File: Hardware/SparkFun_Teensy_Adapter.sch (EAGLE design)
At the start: 17 parts, among them U1 5V

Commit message: Updates for QC final review before reds
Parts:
- FRAME1: VERSION (none) -> v10
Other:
- note added: "v10"
- note removed: "v01"
- moved on the sheet: SJ1, SJ2
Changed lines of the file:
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@@
 <part name="FRAME1" library="SparkFun-Aesthetics" deviceset="FRAME-LETTER" device="">
 <attribute name="DESIGNER" value="Toni Klopfenstein"/>
+<attribute name="VERSION" value="v10"/>
 </part>
 <part name="LOGO1" library="SparkFun-Aesthetics" deviceset="SFE_LOGO_NAME_FLAME" device=".1_INCH"/>
@@
 <part name="GND10" library="SparkFun-Aesthetics" deviceset="GND" device=""/>
 <part name="U1" library="SparkFun-PowerIC" deviceset="V_REG_78XX" device="-TO-220" value="5V"/>
+<part name="SUPPLY1" library="SparkFun-Aesthetics" deviceset="5V" device=""/>
+<part name="SUPPLY2" library="SparkFun-Aesthetics" deviceset="5V" device=""/>
+<part name="SUPPLY3" library="SparkFun-Aesthetics" deviceset="5V" device=""/>
+<part name="SUPPLY4" library="SparkFun-Aesthetics" deviceset="3.3V" device=""/>
+<part name="SUPPLY5" library="SparkFun-Aesthetics" deviceset="3.3V" device=""/>
+<part name="SUPPLY6" library="SparkFun-Aesthetics" deviceset="3.3V" device=""/>
+<part name="SUPPLY7" library="SparkFun-Aesthetics" deviceset="3.3V" device=""/>
 </parts>
 <sheets>
@@
 <text x="157.48" y="170.18" size="1.4224" layer="97">Add 32.768kHZ crystal
 to Teensy for use of RTC.  </text>
-<text x="2.54" y="142.24" size="1.27" layer="97">Cut trace between VUSB and VIN pads
- on Teensy to use external power supply. </text>
-<text x="5.08" y="76.2" size="1.778" layer="97">Jumpers default
+<text x="2.54" y="134.62" size="1.778" layer="97">Cut trace between
+ VUSB and VIN pads
+ on Teensy to use
+external power supply. </text>
+<text x="7.62" y="68.58" size="1.778" layer="97">Jumpers default
 to SDA/SCL.
 Can be adjusted to
-A6/A7 for Leonardo-compatible shields.</text>
+A6/A7 for
+Leonardo-compatible shields.</text>
 <wire x1="142.24" y1="185.42" x2="147.32" y2="185.42" width="0.2032" layer="97" style="shortdash"/>
 <wire x1="147.32" y1="185.42" x2="147.32" y2="147.32" width="0.2032" layer="97" style="shortdash"/>
@@
 <wire x1="106.68" y1="185.42" x2="106.68" y2="127" width="0.2032" layer="97" style="shortdash"/>
 <text x="116.84" y="129.54" size="2.54" layer="97">RTC Battery</text>
-<text x="238.76" y="7.62" size="2.54" layer="94">v01</text>
-<text x="172.72" y="10.16" size="2.54" layer="94">Toni Klopfenstein</text>
+<text x="238.76" y="7.62" size="2.54" layer="94">v10</text>
+<text x="171.958" y="10.922" size="2.54" layer="94">Toni Klopfenstein</text>
 </plain>
 <instances>
@@
 <instance part="GND2" gate="1" x="170.18" y="68.58"/>
 <instance part="GND3" gate="1" x="58.42" y="15.24"/>
-<instance part="SJ1" gate="G$1" x="30.48" y="104.14" smashed="yes" rot="R180">
-<attribute name="NAME" x="27.94" y="103.759" size="1.778" layer="95" rot="R180"/>
-</instance>
-<instance part="SJ2" gate="G$1" x="45.72" y="93.98" smashed="yes" rot="R180">
-<attribute name="NAME" x="43.18" y="93.599" size="1.778" layer="95" rot="R180"/>
+<instance part="SJ1" gate="G$1" x="20.32" y="104.14" smashed="yes" rot="R180">
+<attribute name="NAME" x="17.78" y="103.759" size="1.778" layer="95" rot="R180"/>
+</instance>
+<instance part="SJ2" gate="G$1" x="35.56" y="93.98" smashed="yes" rot="R180">
+<attribute name="NAME" x="33.02" y="93.599" size="1.778" layer="95" rot="R180"/>
 </instance>
 <instance part="JP2" gate="G$1" x="20.32" y="147.32" smashed="yes">
@@
 <instance part="GND10" gate="1" x="129.54" y="17.78"/>
 <instance part="U1" gate="G$1" x="68.58" y="154.94"/>
+<instance part="SUPPLY1" gate="G$1" x="83.82" y="157.48"/>
+<instance part="SUPPLY2" gate="G$1" x="45.72" y="88.9"/>
+<instance part="SUPPLY3" gate="G$1" x="157.48" y="99.06"/>
+<instance part="SUPPLY4" gate="G$1" x="25.4" y="175.26"/>
+<instance part="SUPPLY5" gate="G$1" x="40.64" y="86.36"/>
+<instance part="SUPPLY6" gate="G$1" x="60.96" y="33.02"/>
+<instance part="SUPPLY7" gate="G$1" x="152.4" y="93.98"/>
 </instances>
 <busses>
@@
 <segment>
 <pinref part="SJ2" gate="G$1" pin="3"/>
-<wire x1="45.72" y1="99.06" x2="45.72" y2="101.6" width="0.1524" layer="91"/>
-<wire x1="45.72" y1="101.6" x2="40.64" y2="101.6" width="0.1524" layer="91"/>
-<label x="40.64" y="101.6" size="1.27" layer="95" rot="R180" xref="yes"/>
+<wire x1="35.56" y1="99.06" x2="35.56" y2="101.6" width="0.1524" layer="91"/>
+<wire x1="35.56" y1="101.6" x2="30.48" y2="101.6" width="0.1524" layer="91"/>
+<label x="30.48" y="101.6" size="1.27" layer="95" rot="R180" xref="yes"/>
 </segment>
 </net>
@@
 <segment>
 <pinref part="SJ1" gate="G$1" pin="3"/>
-<wire x1="30.48" y1="109.22" x2="30.48" y2="111.76" width="0.1524" layer="91"/>
-<wire x1="30.48" y1="111.76" x2="25.4" y2="111.76" width="0.1524" layer="91"/>
-<label x="25.4" y="111.76" size="1.27" layer="95" rot="R180" xref="yes"/>
+<wire x1="20.32" y1="109.22" x2="20.32" y2="111.76" width="0.1524" layer="91"/>
+<wire x1="20.32" y1="111.76" x2="15.24" y2="111.76" width="0.1524" layer="91"/>
+<label x="15.24" y="111.76" size="1.27" layer="95" rot="R180" xref="yes"/>
 </segment>
 </net>
@@
 <segment>
 <pinref part="JP10" gate="G$1" pin="3.3V"/>
-<wire x1="63.5" y1="83.82" x2="55.88" y2="83.82" width="0.1524" layer="91"/>
-<label x="55.88" y="83.82" size="1.27" layer="95" rot="R180" xref="yes"/>
+<wire x1="63.5" y1="83.82" x2="40.64" y2="83.82" width="0.1524" layer="91"/>
+<wire x1="40.64" y1="83.82" x2="40.64" y2="86.36" width="0.1524" layer="91"/>
+<pinref part="SUPPLY5" gate="G$1" pin="3.3V"/>
 </segment>
 <segment>
 <pinref part="JP11" gate="G$1" pin="3.3V"/>
-<wire x1="177.8" y1="91.44" x2="170.18" y2="91.44" width="0.1524" layer="91"/>
-<label x="170.18" y="91.44" size="1.27" layer="95" rot="R180" xref="yes"/>
+<wire x1="177.8" y1="91.44" x2="152.4" y2="91.44" width="0.1524" layer="91"/>
+<wire x1="152.4" y1="91.44" x2="152.4" y2="93.98" width="0.1524" layer="91"/>
+<pinref part="SUPPLY7" gate="G$1" pin="3.3V"/>
 </segment>
 <segment>
 <pinref part="JP3" gate="G$1" pin="2"/>
-<wire x1="17.78" y1="172.72" x2="22.86" y2="172.72" width="0.1524" layer="91"/>
-<label x="22.86" y="172.72" size="1.27" layer="95" xref="yes"/>
+<wire x1="17.78" y1="172.72" x2="25.4" y2="172.72" width="0.1524" layer="91"/>
+<wire x1="25.4" y1="172.72" x2="25.4" y2="175.26" width="0.1524" layer="91"/>
+<pinref part="SUPPLY4" gate="G$1" pin="3.3V"/>
 </segment>
 <segment>
 <pinref part="JP9" gate="G$1" pin="2"/>
-<wire x1="53.34" y1="30.48" x2="58.42" y2="30.48" width="0.1524" layer="91"/>
-<label x="58.42" y="30.48" size="1.27" layer="95" xref="yes"/>
+<wire x1="53.34" y1="30.48" x2="60.96" y2="30.48" width="0.1524" layer="91"/>
+<wire x1="60.96" y1="30.48" x2="60.96" y2="33.02" width="0.1524" layer="91"/>
+<pinref part="SUPPLY6" gate="G$1" pin="3.3V"/>
 </segment>
 </net>
@@
 <segment>
 <pinref part="JP10" gate="G$1" pin="A4"/>
-<wire x1="63.5" y1="104.14" x2="35.56" y2="104.14" width="0.1524" layer="91"/>
+<wire x1="63.5" y1="104.14" x2="25.4" y2="104.14" width="0.1524" layer="91"/>
 <pinref part="SJ1" gate="G$1" pin="2"/>
 </segment>
@@
 <segment>
 <pinref part="SJ2" gate="G$1" pin="2"/>
-<wire x1="50.8" y1="93.98" x2="55.88" y2="93.98" width="0.1524" layer="91"/>
-<wire x1="55.88" y1="93.98" x2="55.88" y2="101.6" width="0.1524" layer="91"/>
+<wire x1="40.64" y1="93.98" x2="43.18" y2="93.98" width="0.1524" layer="91"/>
+<wire x1="43.18" y1="93.98" x2="43.18" y2="101.6" width="0.1524" layer="91"/>
 <pinref part="JP10" gate="G$1" pin="A5"/>
-<wire x1="55.88" y1="101.6" x2="63.5" y2="101.6" width="0.1524" layer="91"/>
+<wire x1="43.18" y1="101.6" x2="63.5" y2="101.6" width="0.1524" layer="91"/>
 </segment>
 </net>
@@
 <segment>
 <pinref part="JP11" gate="G$1" pin="VIN"/>
-<wire x1="177.8" y1="96.52" x2="170.18" y2="96.52" width="0.1524" layer="91"/>
-<label x="170.18" y="96.52" size="1.27" layer="95" rot="R180" xref="yes"/>
+<wire x1="177.8" y1="96.52" x2="157.48" y2="96.52" width="0.1524" layer="91"/>
+<wire x1="157.48" y1="96.52" x2="157.48" y2="99.06" width="0.1524" layer="91"/>
+<pinref part="SUPPLY3" gate="G$1" pin="5V"/>
 </segment>
 <segment>
 <pinref part="JP10" gate="G$1" pin="5V"/>
-<wire x1="63.5" y1="86.36" x2="55.88" y2="86.36" width="0.1524" layer="91"/>
-<label x="55.88" y="86.36" size="1.27" layer="95" rot="R180" xref="yes"/>
-</segment>
-<segment>
-<label x="81.28" y="154.94" size="1.27" layer="95" xref="yes"/>
+<wire x1="63.5" y1="86.36" x2="45.72" y2="86.36" width="0.1524" layer="91"/>
+<wire x1="45.72" y1="86.36" x2="45.72" y2="88.9" width="0.1524" layer="91"/>
+<pinref part="SUPPLY2" gate="G$1" pin="5V"/>
+</segment>
+<segment>
 <pinref part="U1" gate="G$1" pin="OUT"/>
-<wire x1="76.2" y1="154.94" x2="81.28" y2="154.94" width="0.1524" layer="91"/>
+<wire x1="76.2" y1="154.94" x2="83.82" y2="154.94" width="0.1524" layer="91"/>
+<wire x1="83.82" y1="154.94" x2="83.82" y2="157.48" width="0.1524" layer="91"/>
+<pinref part="SUPPLY1" gate="G$1" pin="5V"/>
 </segment>
 </net>
@@
 <segment>
 <pinref part="SJ1" gate="G$1" pin="1"/>
-<wire x1="30.48" y1="99.06" x2="30.48" y2="93.98" width="0.1524" layer="91"/>
-<wire x1="30.48" y1="93.98" x2="20.32" y2="93.98" width="0.1524" layer="91"/>
-<label x="20.32" y="93.98" size="1.27" layer="95" rot="R180" xref="yes"/>
+<wire x1="20.32" y1="99.06" x2="20.32" y2="93.98" width="0.1524" layer="91"/>
+<wire x1="20.32" y1="93.98" x2="10.16" y2="93.98" width="0.1524" layer="91"/>
+<label x="10.16" y="93.98" size="1.27" layer="95" rot="R180" xref="yes"/>
 </segment>
 <segment>
@@
 <segment>
 <pinref part="SJ2" gate="G$1" pin="1"/>
-<wire x1="45.72" y1="88.9" x2="45.72" y2="83.82" width="0.1524" layer="91"/>
-<wire x1="45.72" y1="83.82" x2="33.02" y2="83.82" width="0.1524" layer="91"/>
-<label x="33.02" y="83.82" size="1.27" layer="95" rot="R180" xref="yes"/>
-</segment>
-<segment>
+<wire x1="35.56" y1="88.9" x2="35.56" y2="83.82" width="0.1524" layer="91"/>
+<wire x1="35.56" y1="83.82" x2="22.86" y2="83.82" width="0.1524" layer="91"/>
+<label x="22.86" y="83.82" size="1.27" layer="95" rot="R180" xref="yes"/>
+</segment>
+<segment>

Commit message: Value Changes for 3D Modeling
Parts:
- BAT1: value (none) -> CoinCell
- JP3: value (none) -> JST2
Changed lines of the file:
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@@
 <?xml version="1.0" encoding="utf-8"?>
 <!DOCTYPE eagle SYSTEM "eagle.dtd">
-<eagle version="7.2.0">
+<eagle version="7.7.0">
 <drawing>
 <settings>
@@
 <part name="JP2" library="SparkFun-Connectors" deviceset="POWER_JACK" device="PTH_LOCK"/>
 <part name="GND5" library="SparkFun-Aesthetics" deviceset="GND" device=""/>
-<part name="JP3" library="SparkFun-Connectors" deviceset="M02" device="JST-PTH-2"/>
+<part name="JP3" library="SparkFun-Connectors" deviceset="M02" device="JST-PTH-2" value="JST2"/>
 <part name="GND6" library="SparkFun-Aesthetics" deviceset="GND" device=""/>
 <part name="GND7" library="SparkFun-Aesthetics" deviceset="GND" device=""/>
@@
 <part name="JP8" library="SparkFun-Connectors" deviceset="M04" device="PTH"/>
 <part name="GND9" library="SparkFun-Aesthetics" deviceset="GND" device=""/>
-<part name="BAT1" library="SparkFun-Electromechanical" deviceset="BATTERY" device="12PTH"/>
+<part name="BAT1" library="SparkFun-Electromechanical" deviceset="BATTERY" device="12PTH" value="CoinCell"/>
 <part name="GND4" library="SparkFun-Aesthetics" deviceset="GND" device=""/>
 <part name="JP1" library="SparkFun-Connectors" deviceset="M02" device="PTH"/>

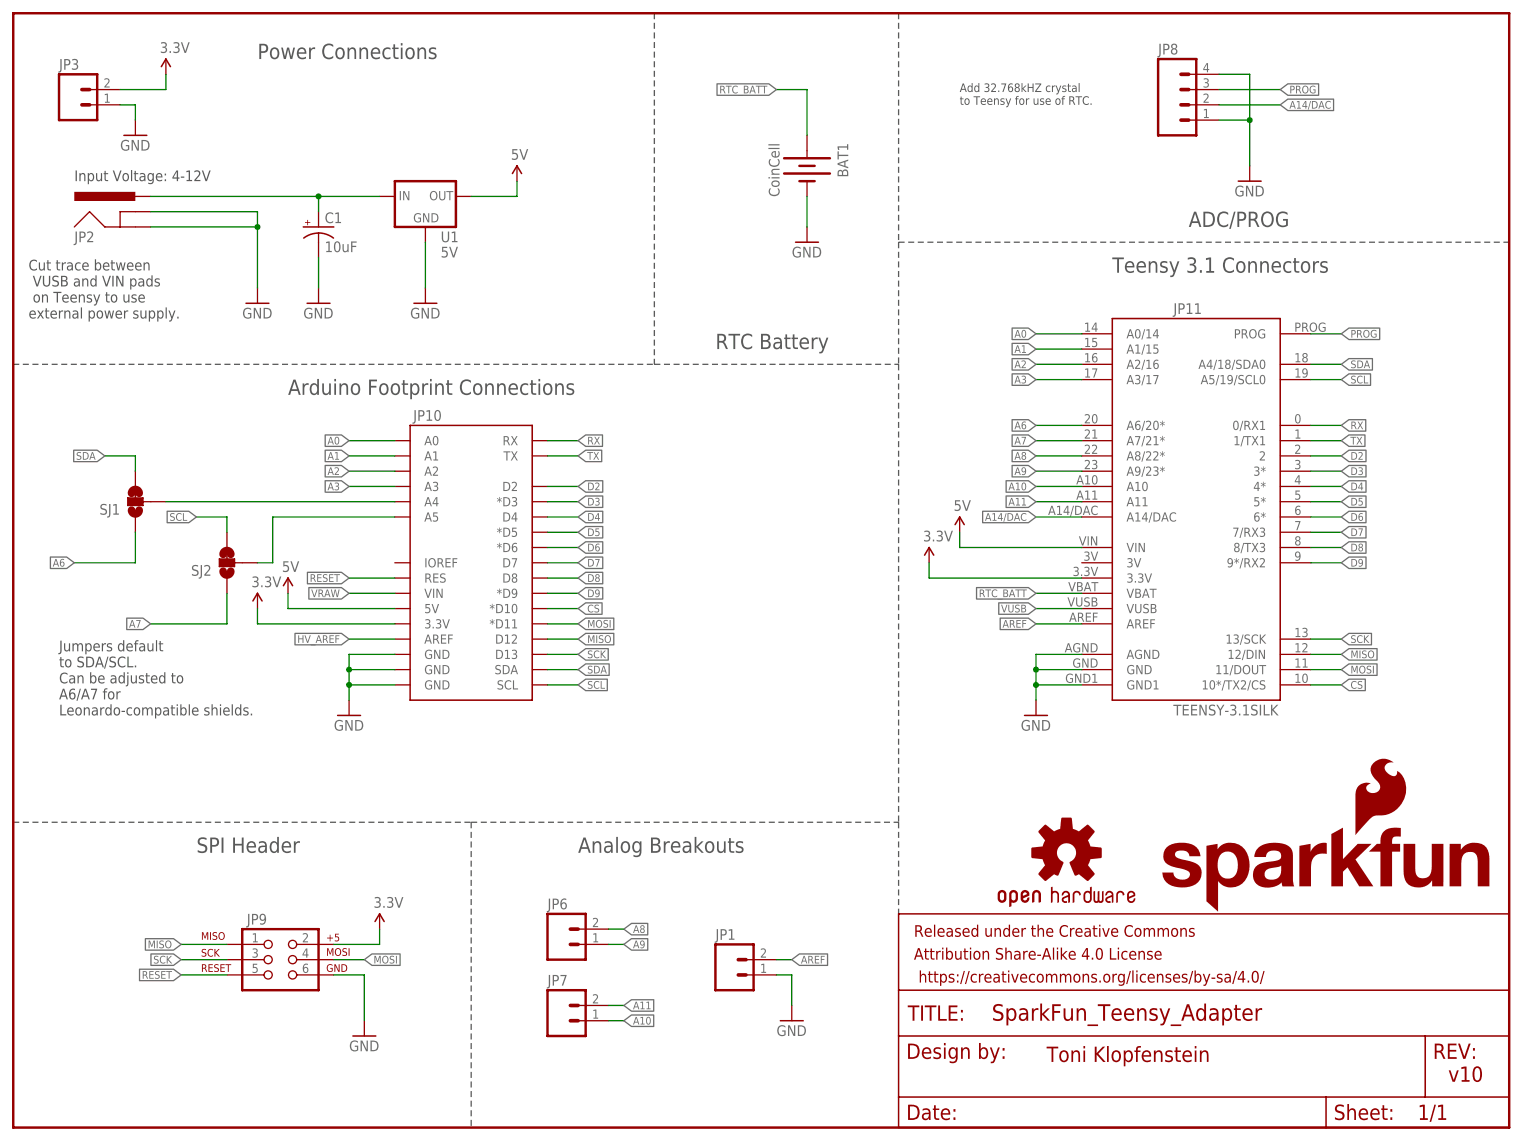
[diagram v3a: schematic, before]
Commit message: Remove ISP connection to 3.3V. Add NO jumper connection.
Request by PaulS. When a shield was attached via SPI the 5V from the shield would kill the 3.3V Teensy.
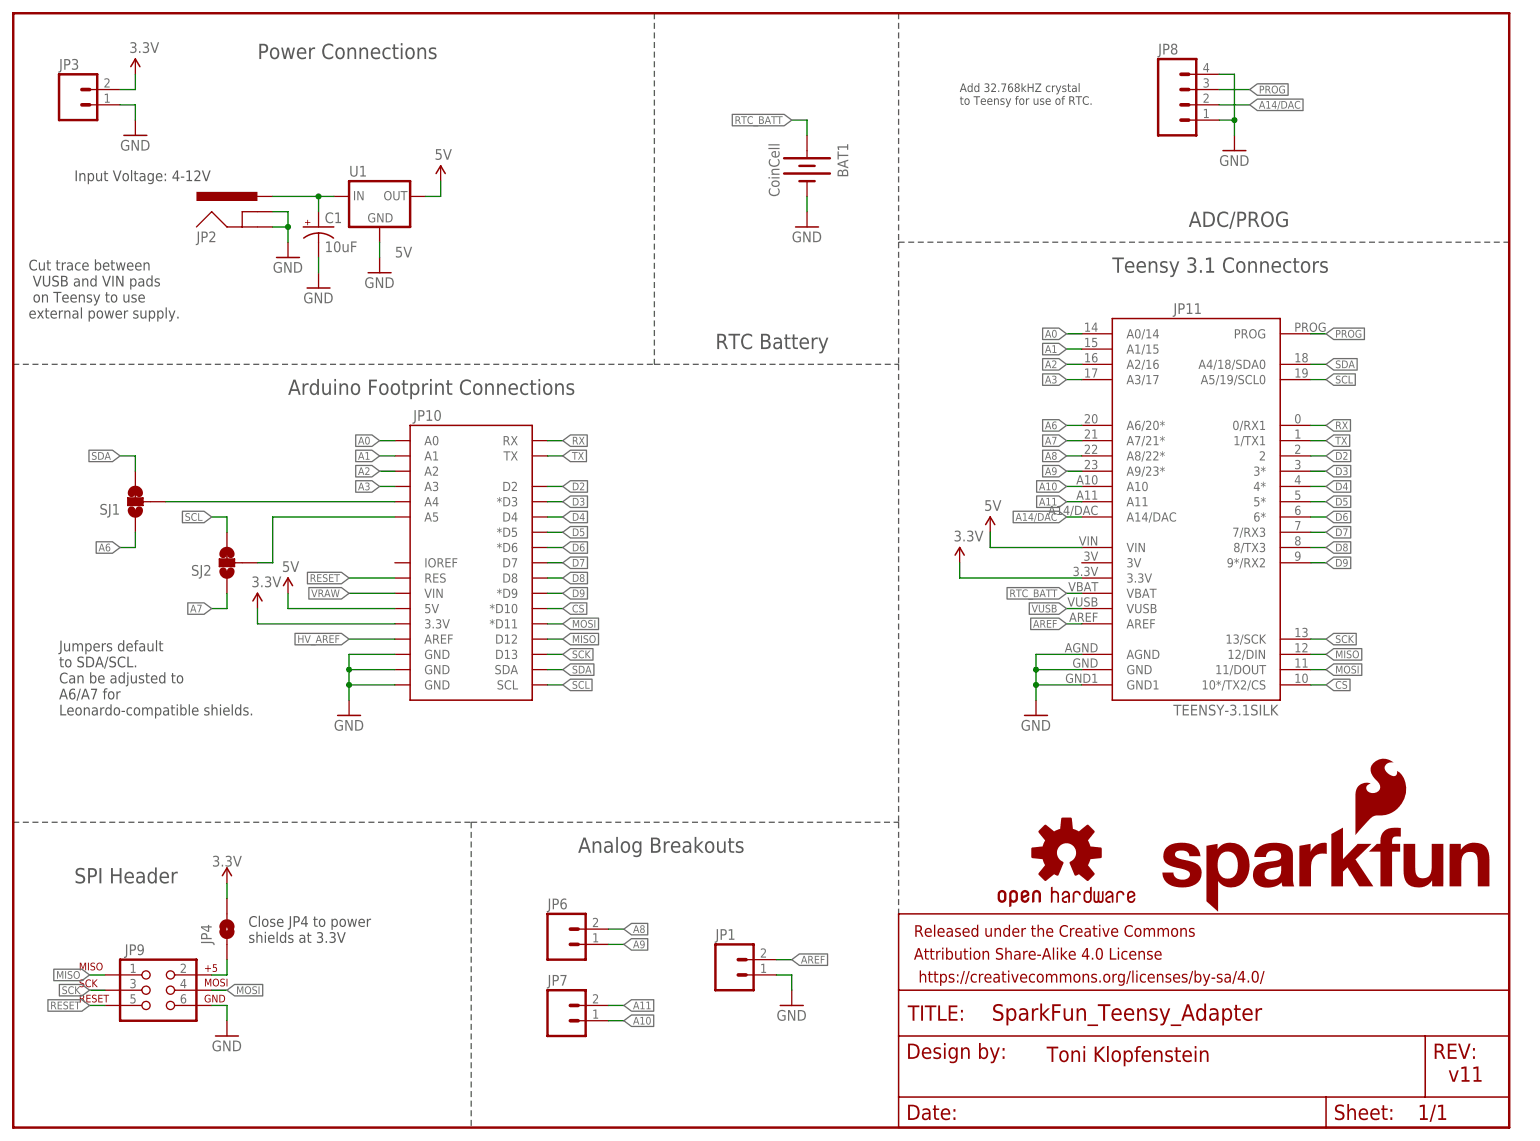
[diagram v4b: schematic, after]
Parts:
- added JP4: JUMPER-SMT_2_NO_SILK, SparkFun-Jumpers:JUMPER-SMT_2_NO_SILK
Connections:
- new net N$1: JP4.1, JP9.2
- net 3.3V: now also JP4.2; no longer JP9.2
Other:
- note added: "Close JP4 to power shields at 3.3V"
- note added: "v11"
- note removed: "v10"
- moved on the sheet: JP2, JP9, U1

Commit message: Getting sch and brd consistant.
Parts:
- FRAME1: value (none) -> FRAME-LETTER; DESIGNER Toni Klopfenstein -> (none); VERSION v10 -> (none)
